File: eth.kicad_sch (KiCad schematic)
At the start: 58 parts, among them U1901 KSZ9131RNXC, Y1901 Resonator_25MHz_ECX-1247Q

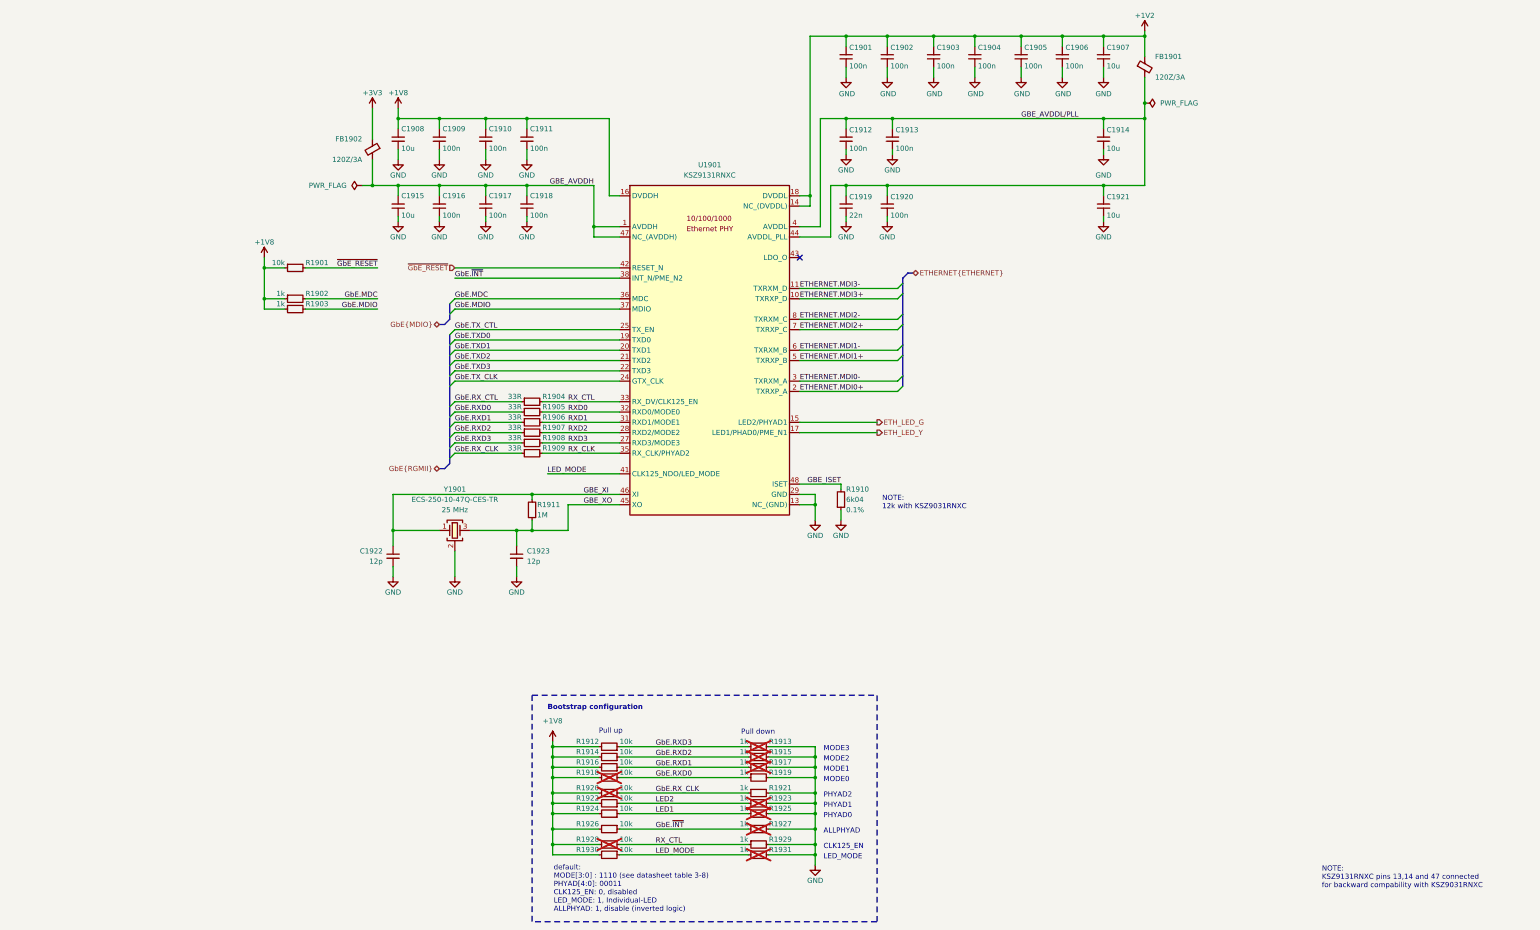
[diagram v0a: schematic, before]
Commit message: [#100282] Add missing schematic sheet names and align them all
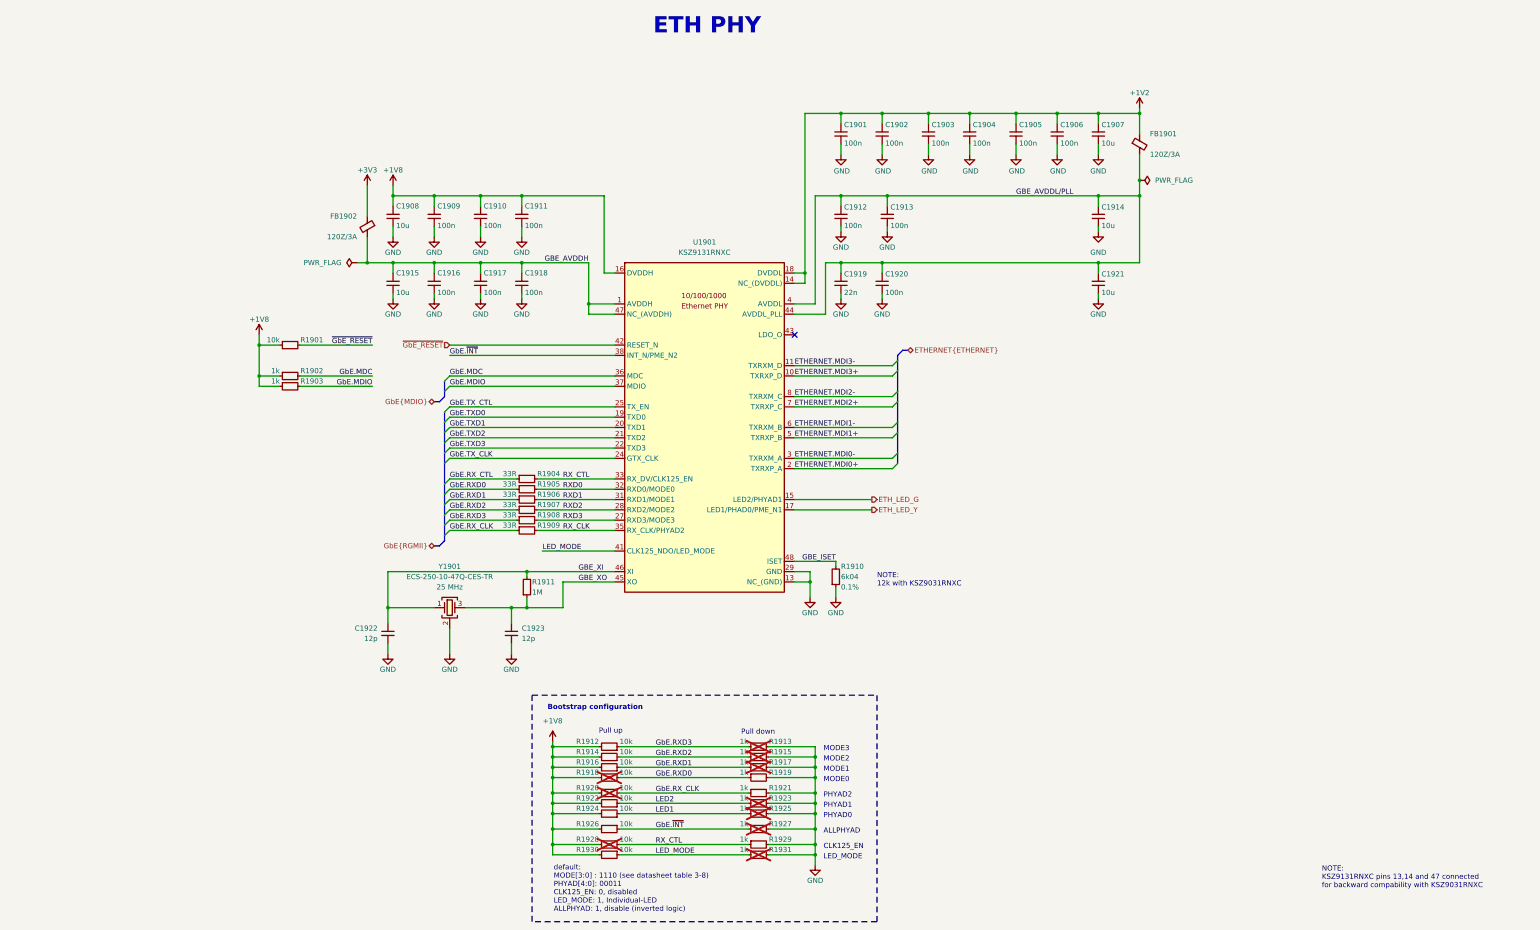
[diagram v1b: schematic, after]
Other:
- note added: "ETH PHY"
- moved on the sheet: C1901, C1902, C1903, C1904, C1905, C1906, C1907, C1908, C1909, C1910, C1911, C1912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

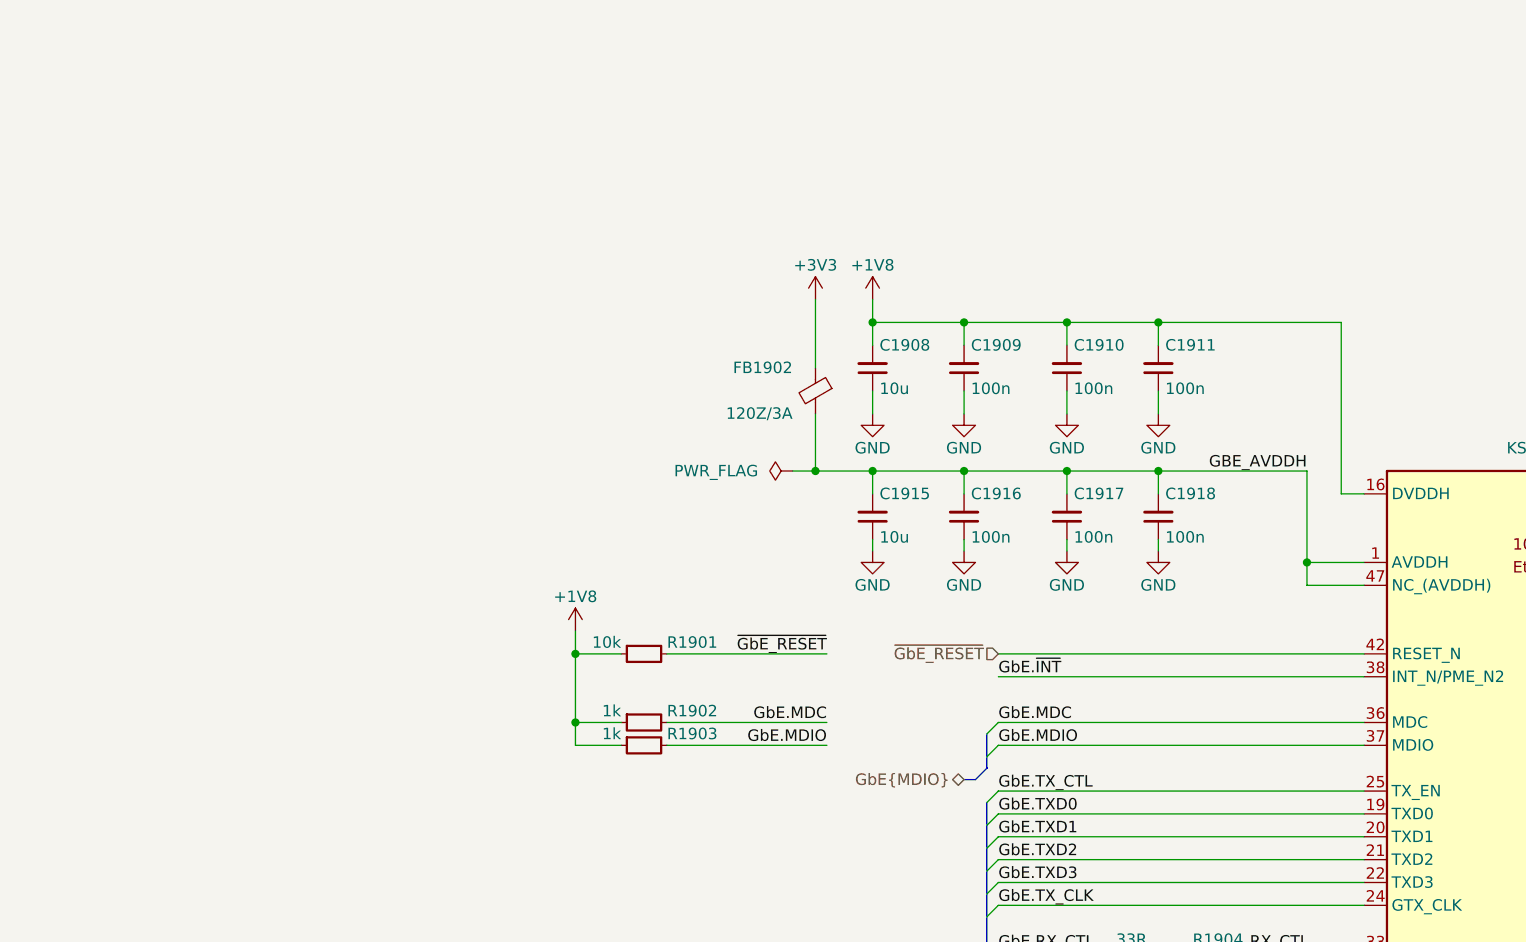
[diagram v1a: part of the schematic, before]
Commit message: [#100501] Gate GbE_PHY_RESET with COLD_RESET signal, to reset ETH PHY
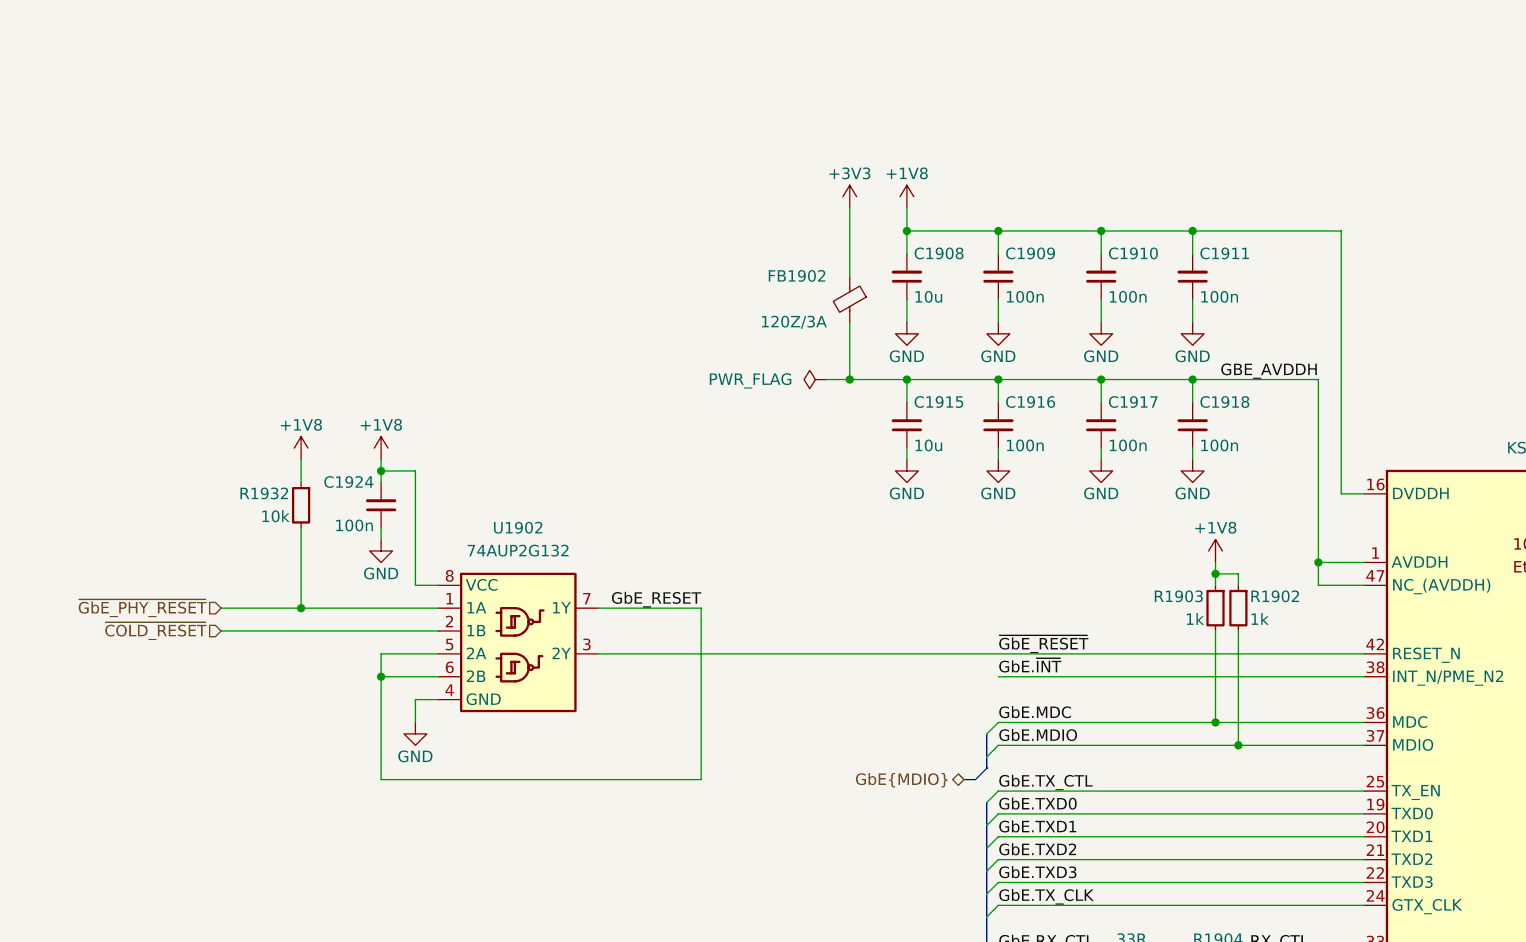
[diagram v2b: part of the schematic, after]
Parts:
- removed R1901: R_10k_0402, antmicro-footprints:R_0402_1005Metric, symbol antmicroResistors0402:R_10k_0402
- added C1924: C_100n_0402, antmicro-footprints:C_0402_1005Metric, symbol antmicroCapacitors0402:C_100n_0402
- added R1932: R_10k_0402, antmicro-footprints:R_0402_1005Metric, symbol antmicroResistors0402:R_10k_0402
- added U1902: 74AUP2G132, antmicro-footprints:VSSOP-8_2.3x2mm_P0.5mm, symbol antmicroLogicGatesandInverters:74AUP2G132
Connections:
- net +1V8: now also C1924.2, R1932.1, U1902.8 (VCC)
- net GND: now also C1924.1, U1902.4 (GND)
- net GbE.MDC: now also R1903.2; no longer R1902.2
- net GbE.MDIO: now also R1902.2; no longer R1903.2
- net ~{GbE_RESET}: now also U1902.3 (2Y)
- new net GbE_RESET: U1902.5 (2A), U1902.6 (2B), U1902.7 (1Y)
- new net ~{COLD_RESET}: U1902.2 (1B)
- new net ~{GbE_PHY_RESET}: R1932.2, U1902.1 (1A)
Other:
- moved on the sheet: C1908, C1909, C1910, C1911, C1915, C1916, C1917, C1918, FB1902

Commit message: [#100501] DNP GbE_INT pullup resistor leaving this signal floating
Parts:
- R1926: now not fitted
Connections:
- net GbE.~{INT} renamed ~{GbE_INT}
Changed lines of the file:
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@@
-		)
-	)
-	(label "GbE.~{INT}"
-		(at 198.12 236.22 0)
-		(effects
-			(font
-				(size 1.27 1.27)
-			)
-			(justify left bottom)
 		)
 	)
@@
 		)
 	)
-	(label "GbE.~{INT}"
+	(label "~{GbE_INT}"
+		(at 198.12 236.22 0)
+		(effects
+			(font
+				(size 1.27 1.27)
+			)
+			(justify left bottom)
+		)
+	)
+	(label "~{GbE_INT}"
 		(at 147.32 119.38 0)
 		(effects
@@
 		(on_board yes)
 		(in_pos_files yes)
-		(dnp no)
+		(dnp yes)
 		(property "Reference" "R1926"
 			(at 184.15 234.95 0)

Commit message: [#100501] Add level shifter for ETH LEDs
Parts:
- added C1927, C1928: C_100n_0402, antmicro-footprints:C_0402_1005Metric, symbol antmicroCapacitors0402:C_100n_0402
- added U1904: TXU0304BQAR, antmicro-footprints:DHVQFN-14-1EP_2.5x3mm, symbol antmicroLogicTranslatorsLevelShifters:TXU0304BQAR
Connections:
- net +1V8: now also C1928.2, U1904.1 (VCCA)
- net +3V3: now also C1927.2, U1904.14 (VCCB), U1904.8 (OE)
- net ETH_LED_G: now also U1904.13 (B1Y); no longer U1901.15 (LED2/PHYAD1)
- net ETH_LED_Y: now also U1904.12 (B2Y); no longer U1901.17 (LED1/PHAD0/PME_N1)
- net GND: now also C1927.1, C1928.1, U1904.15 (GND), U1904.7 (GND)
- net LED1: now also U1901.17 (LED1/PHAD0/PME_N1), U1904.3 (A2)
- net LED2: now also U1901.15 (LED2/PHYAD1), U1904.2 (A1)
- no-connect marks 1 -> 5

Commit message: [#100501] Reannotate schematic
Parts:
- renumbered C1901 to C155, C1902 to C156, C1903 to C157, C1904 to C158, C1905 to C159, C1906 to C160, C1907 to C161, C1908 to C162, C1909 to C163, C1910 to C164, C1911 to C165, C1912 to C166, C1913 to C167, C1914 to C168, C1915 to C169, C1916 to C170, C1917 to C171, C1918 to C172, C1924 to C173, C1919 to C174, C1920 to C175, C1921 to C176, C1928 to C177, C1927 to C178, C1922 to C179, C1923 to C180, FB1901 to FB2, FB1902 to FB3, R1932 to R188, R1903 to R189, R1902 to R190, R1904 to R191, R1905 to R192, R1906 to R193, R1907 to R194, R1908 to R195, R1909 to R196, R1910 to R197, R1911 to R198, R1912 to R199, R1913 to R200, R1914 to R201, R1915 to R202, R1916 to R203, R1917 to R204, R1918 to R205, R1919 to R206, R1920 to R207, R1921 to R208, R1922 to R209, R1923 to R210, R1924 to R211, R1925 to R212, R1926 to R213, R1927 to R214, R1928 to R215, R1929 to R216, R1930 to R217, R1931 to R218, U1901 to U24, U1902 to U25, U1904 to U26, Y1901 to Y5

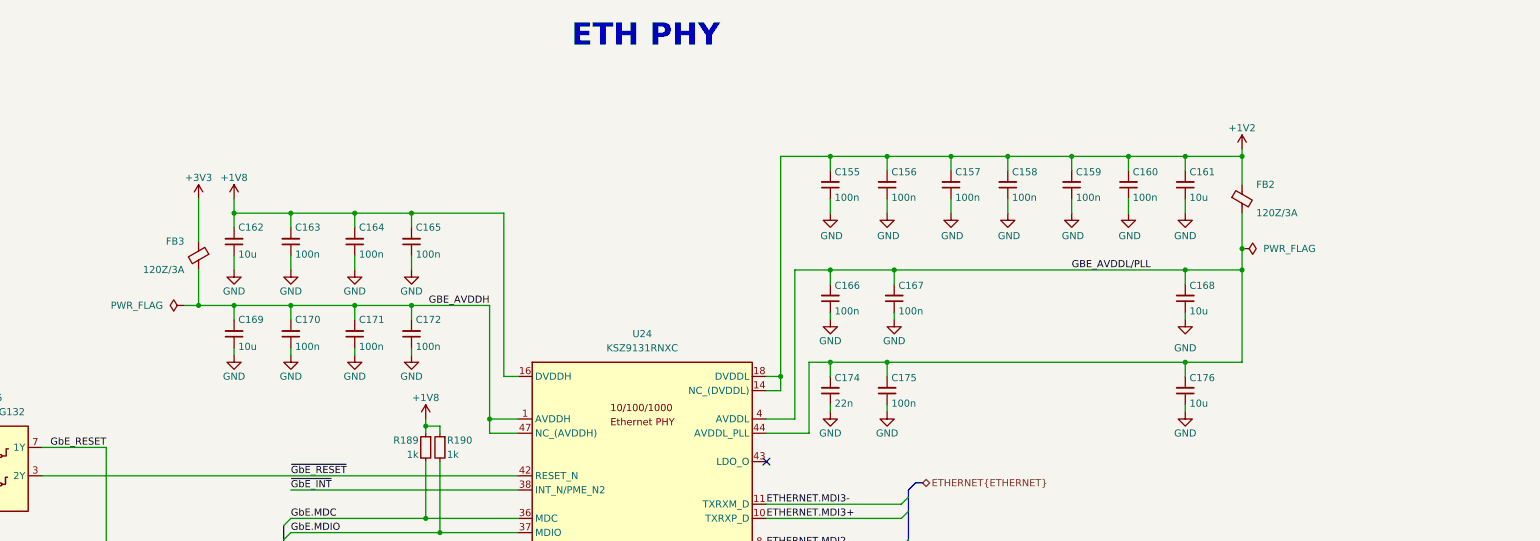
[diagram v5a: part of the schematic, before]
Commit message: [#100501] Add ferrite beads to ETH PHY
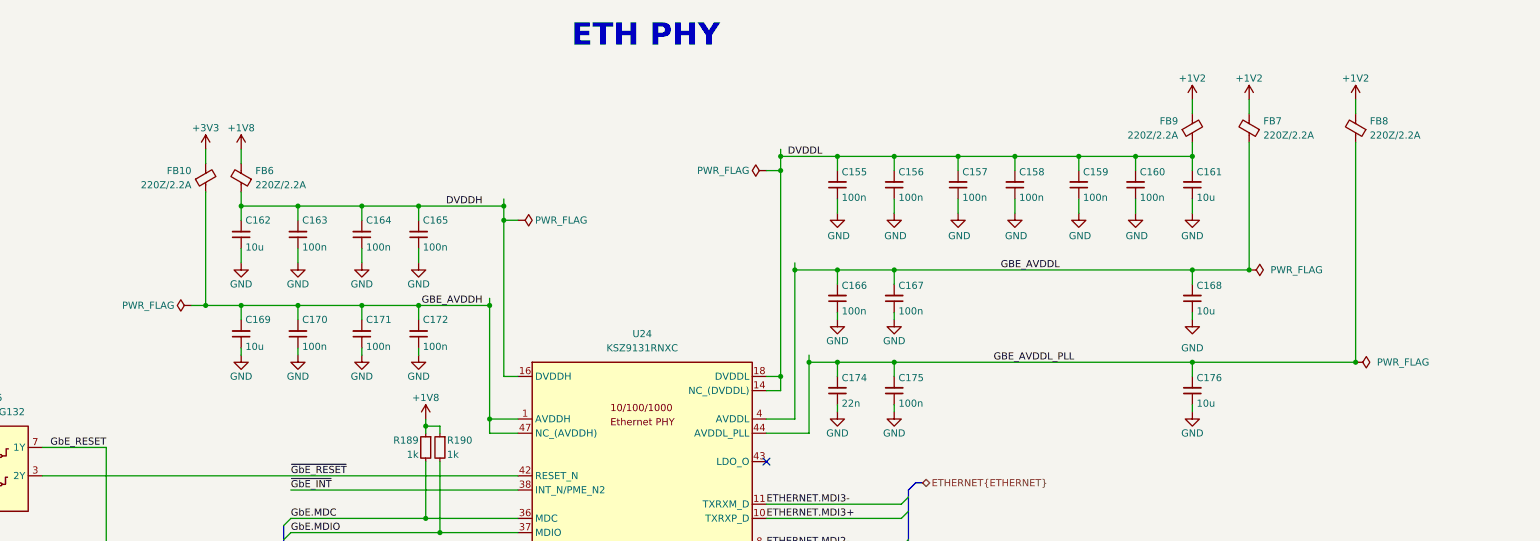
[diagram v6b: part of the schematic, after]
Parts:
- removed FB2, FB3: FB_120Z_3A_Murata-BLM18SG_0603, antmicro-footprints:FB_0603_1608Metric, symbol antmicroFerriteBeadsandChips:FB_120Z_3A_Murata-BLM18SG_0603
- added FB10, FB6, FB7, FB8, FB9: FB_220Z_2.2A_TDK-MPZ_0603, antmicro-footprints:FB_0603_1608Metric, symbol antmicroFerriteBeadsandChips:FB_220Z_2.2A_TDK-MPZ_0603
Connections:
- net +1V2: now also FB7.2, FB8.2, FB9.2; no longer C155.2, C156.2, C157.2, C158.2, C159.2, C160.2, C161.2, U24.14 (NC_(DVDDL)), U24.18 (DVDDL), U24.23 (DVDDL), U24.26 (DVDDL), U24.30 (DVDDL), U24.39 (DVDDL)
- net +1V8: now also FB6.2; no longer C162.2, C163.2, C164.2, C165.2, U24.16 (DVDDH), U24.34 (DVDDH), U24.40 (DVDDH)
- net +3V3: now also FB10.2
- net GBE_AVDDH: now also FB10.1
- net GBE_AVDDL/PLL renamed GBE_AVDDL
- net GBE_AVDDL: now also FB7.1; no longer C174.2, C175.2, C176.2, U24.44 (AVDDL_PLL)
- new net DVDDH: C162.2, C163.2, C164.2, C165.2, FB6.1, U24.16 (DVDDH), U24.34 (DVDDH), U24.40 (DVDDH)
- new net DVDDL: C155.2, C156.2, C157.2, C158.2, C159.2, C160.2, C161.2, FB9.1, U24.14 (NC_(DVDDL)), U24.18 (DVDDL), U24.23 (DVDDL), U24.26 (DVDDL), U24.30 (DVDDL), U24.39 (DVDDL)
- new net GBE_AVDDL_PLL: C174.2, C175.2, C176.2, FB8.1, U24.44 (AVDDL_PLL)
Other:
- moved on the sheet: C155, C156, C157, C158, C159, C160, C161, C162, C163, C164, C165, C166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

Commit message: [#100501] Reannotate schematic
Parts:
- renumbered C155 to C160, C156 to C161, C157 to C162, C158 to C163, C159 to C164, C160 to C165, C161 to C166, C162 to C167, C163 to C168, C164 to C169, C165 to C170, C166 to C171, C167 to C172, C168 to C173, C169 to C174, C170 to C175, C171 to C176, C172 to C177, C173 to C178, C174 to C179, C175 to C180, C176 to C181, C177 to C182, C178 to C183, C179 to C184, C180 to C185, FB9 to FB3, FB7 to FB4, FB8 to FB5, FB10 to FB6, FB6 to FB7, R188 to R233, R189 to R234, R190 to R235, R191 to R236, R192 to R237, R193 to R238, R194 to R239, R195 to R240, R196 to R241, R197 to R242, R198 to R243, R199 to R244, R200 to R245, R201 to R246, R202 to R247, R203 to R248, R204 to R249, R205 to R250, R206 to R251, R207 to R252, R208 to R253, R209 to R254, R210 to R255, R211 to R256, R212 to R257, R213 to R258, R214 to R259, R215 to R260, R216 to R261, R217 to R262, R218 to R263, U24 to U23, U25 to U24, U26 to U25
